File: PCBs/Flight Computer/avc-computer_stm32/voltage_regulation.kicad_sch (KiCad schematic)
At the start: 20 parts, among them IC1 MP2307, U7 LD1117S33TR_SOT223

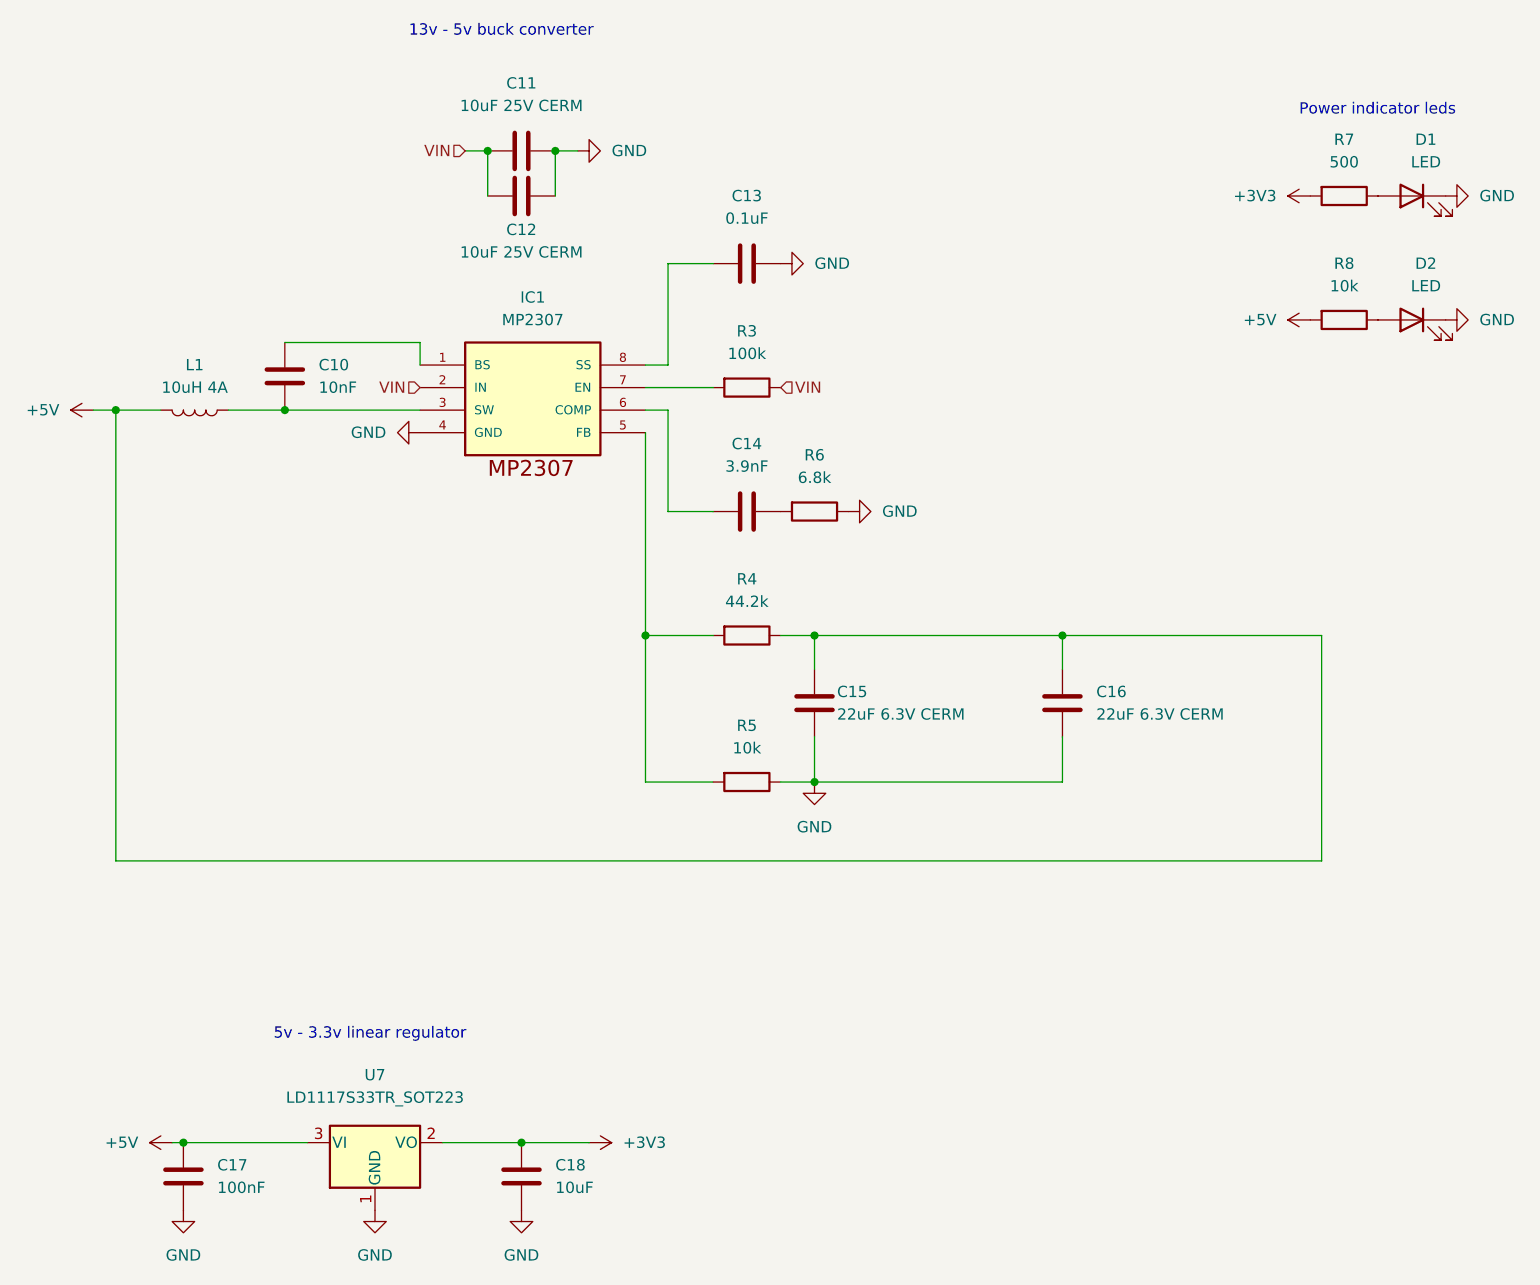
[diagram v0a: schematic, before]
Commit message: Renamed folder
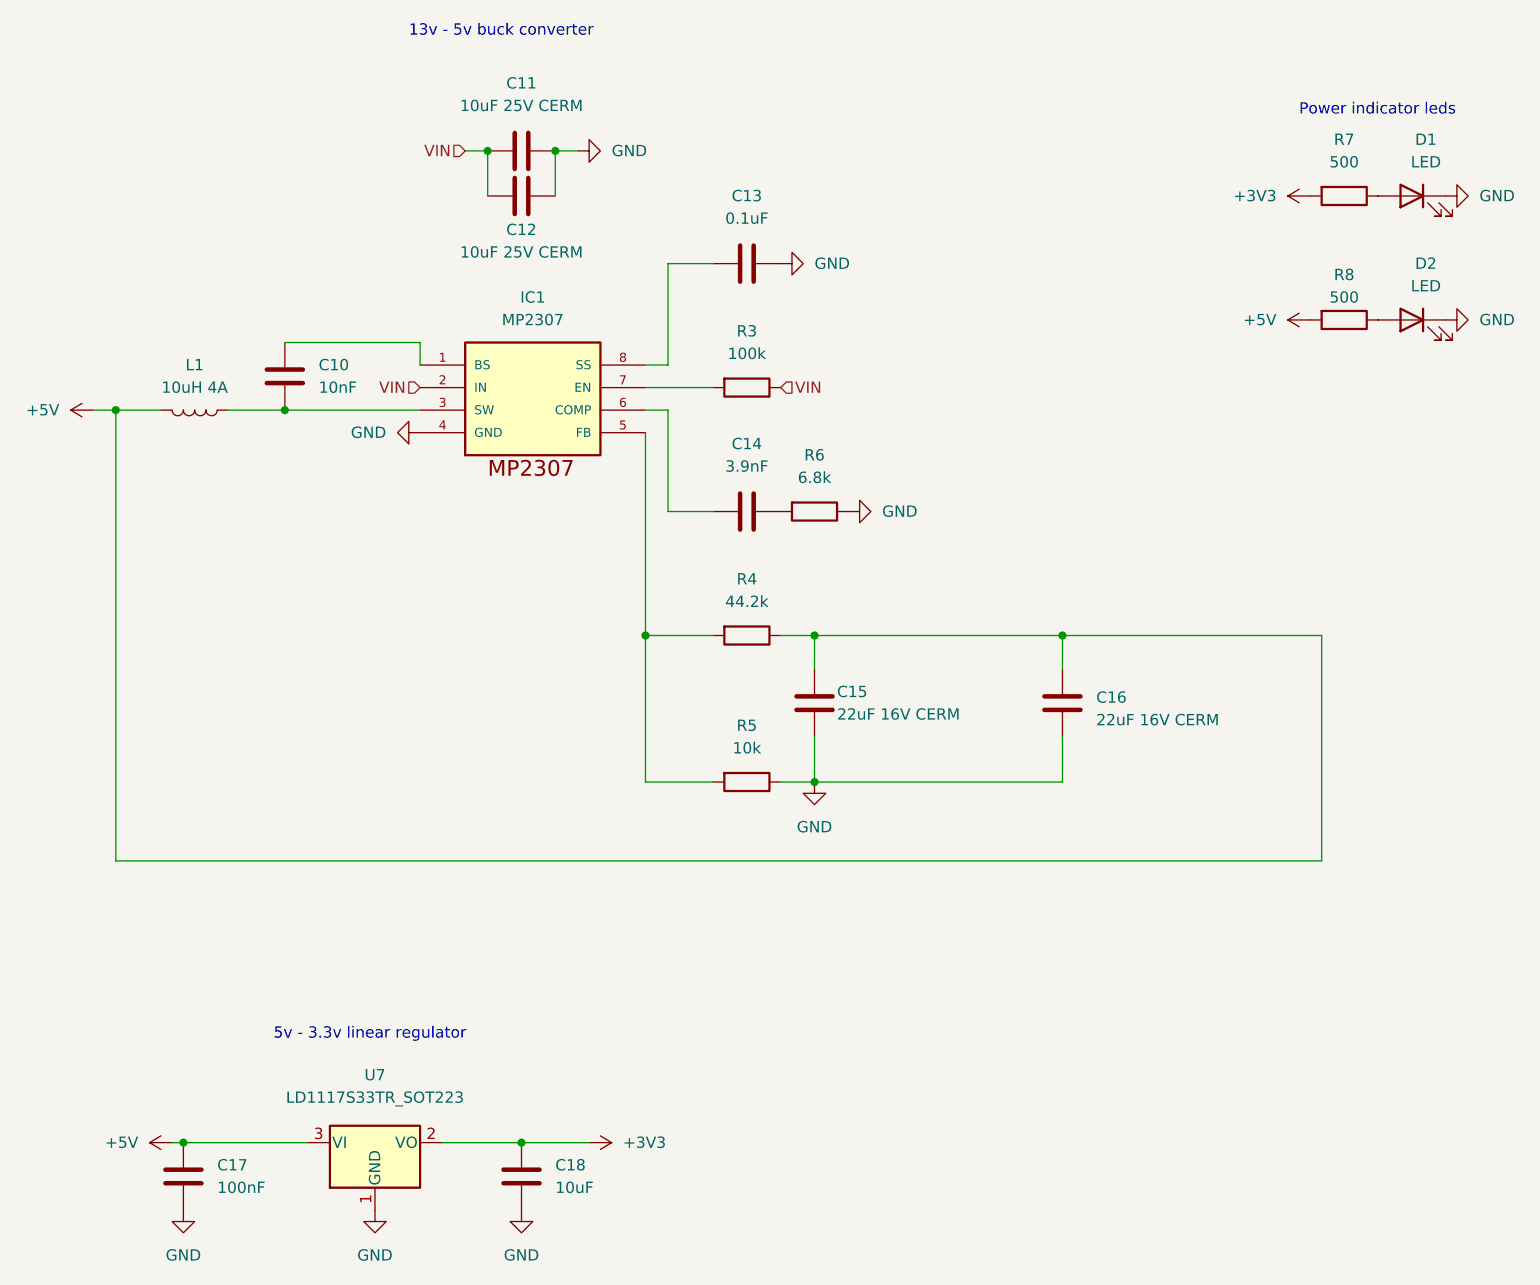
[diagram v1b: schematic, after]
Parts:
- C15, C16: value 22uF 6.3V CERM -> 22uF 16V CERM
- R8: value 10k -> 500
